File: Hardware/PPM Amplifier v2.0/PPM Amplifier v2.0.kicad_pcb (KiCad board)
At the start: 2 copper layers, 0 parts

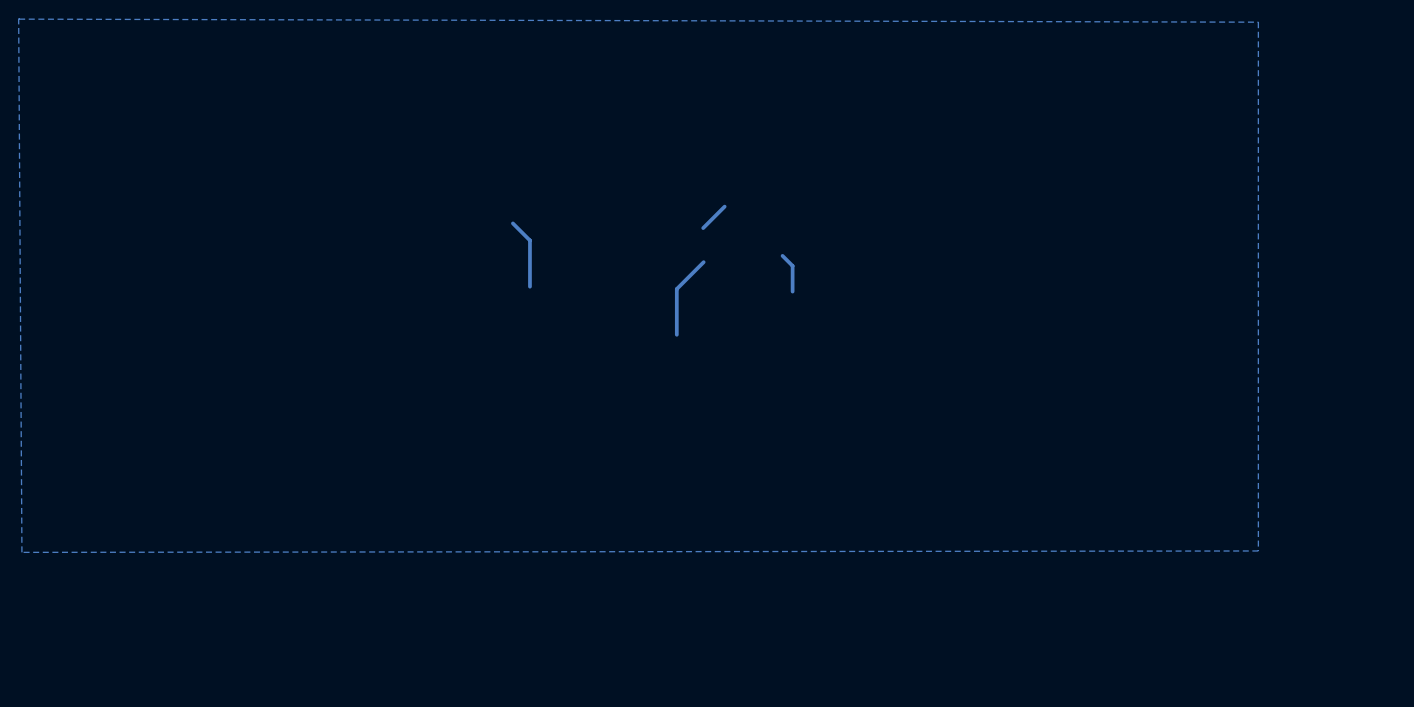
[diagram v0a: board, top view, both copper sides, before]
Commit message: Update PPM Amplifier v2.0 hardware design and add Gerber outputs
Updated KiCad schematic and PCB layout; added fabrication outputs
(Gerber files, drill files, PCBWay BOM/positions/netlist).

Co-Authored-By: Claude Sonnet 4.6 <noreply@anthropic.com>
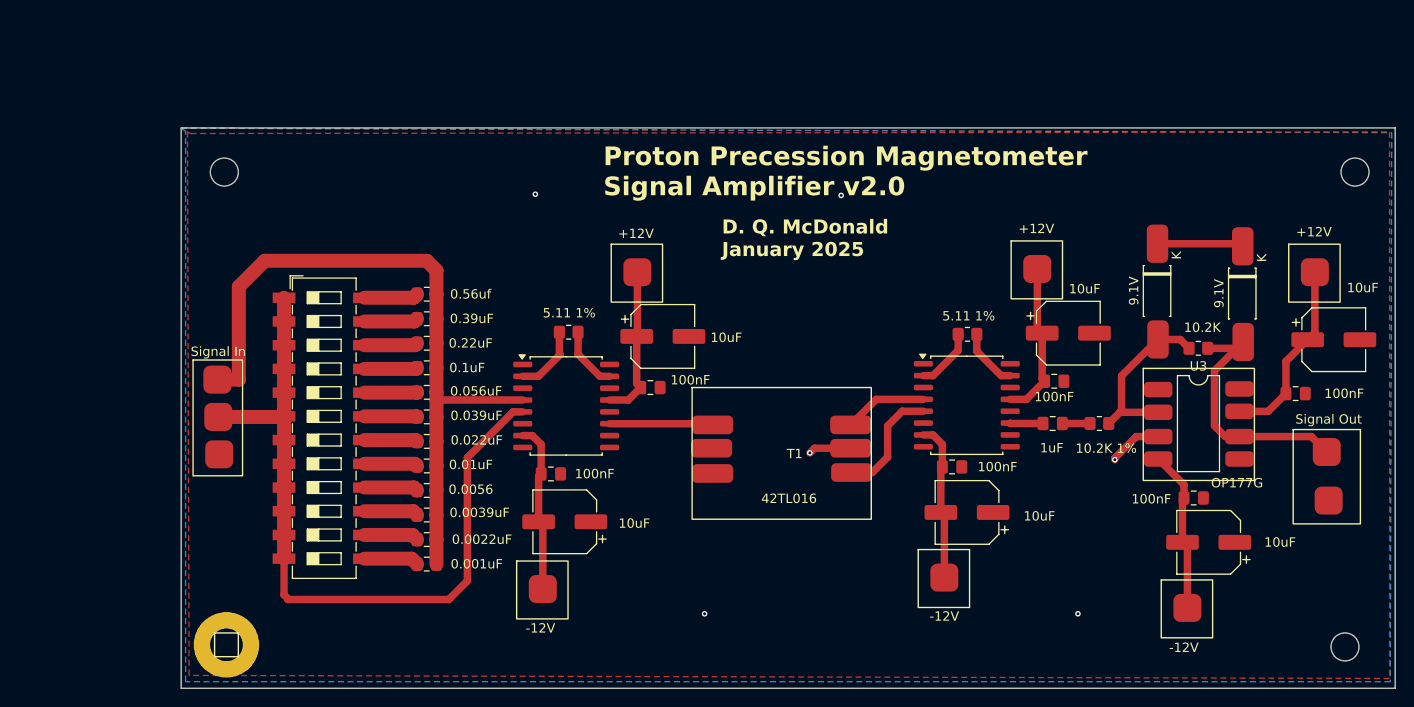
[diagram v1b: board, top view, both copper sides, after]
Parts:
- added C1: 0.56uf, Capacitor_SMD:C_0805_2012Metric_Pad1.18x1.45mm_HandSolder, F.Cu at (70.1, 49.3)
- added C10: 0.0039uF, Capacitor_SMD:C_0805_2012Metric_Pad1.18x1.45mm_HandSolder, F.Cu at (70.1, 72.9)
- added C11: 0.0022uF, Capacitor_SMD:C_0805_2012Metric_Pad1.18x1.45mm_HandSolder, F.Cu at (70.1, 75.5)
- added C12: 0.001uF, Capacitor_SMD:C_0805_2012Metric_Pad1.18x1.45mm_HandSolder, F.Cu at (70.1, 78.2)
- added C13: 10uF, Capacitor_SMD:CP_Elec_6.3x5.2, F.Cu at (95.4, 53.8)
- added C14: 10uF, Capacitor_SMD:CP_Elec_6.3x5.2, F.Cu at (84.9, 73.6)
- added C15: 10uF, Capacitor_SMD:CP_Elec_6.3x5.2, F.Cu at (138.8, 53.4)
- added C16: 10uF, Capacitor_SMD:CP_Elec_6.3x5.2, F.Cu at (167.2, 54.1)
- added C17: 1uF, Capacitor_SMD:C_0805_2012Metric_Pad1.18x1.45mm_HandSolder, F.Cu at (137.1, 63.1)
- added C18: 10uF, Capacitor_SMD:CP_Elec_6.3x5.2, F.Cu at (128.0, 72.6)
- added C19: 10uF, Capacitor_SMD:CP_Elec_6.3x5.2, F.Cu at (153.8, 75.8)
- added C2: 0.39uF, Capacitor_SMD:C_0805_2012Metric_Pad1.18x1.45mm_HandSolder, F.Cu at (70.1, 51.9)
- added C20: 100nF, Capacitor_SMD:C_0805_2012Metric_Pad1.18x1.45mm_HandSolder, F.Cu at (94.0, 59.2)
- added C21: 100nF, Capacitor_SMD:C_0805_2012Metric_Pad1.18x1.45mm_HandSolder, F.Cu at (83.4, 68.5)
- added C22: 100nF, Capacitor_SMD:C_0805_2012Metric_Pad1.18x1.45mm_HandSolder, F.Cu at (152.2, 71.1)
- added C23: 100nF, Capacitor_SMD:C_0805_2012Metric_Pad1.18x1.45mm_HandSolder, F.Cu at (137.3, 58.6)
- added C24: 100nF, Capacitor_SMD:C_0805_2012Metric_Pad1.18x1.45mm_HandSolder, F.Cu at (163.1, 59.9)
- added C25: 100nF, Capacitor_SMD:C_0805_2012Metric_Pad1.18x1.45mm_HandSolder, F.Cu at (126.3, 67.8)
- added C3: 0.22uF, Capacitor_SMD:C_0805_2012Metric_Pad1.18x1.45mm_HandSolder, F.Cu at (70.1, 54.5)
- added C4: 0.1uF, Capacitor_SMD:C_0805_2012Metric_Pad1.18x1.45mm_HandSolder, F.Cu at (70.1, 57.1)
- added C5: 0.056uF, Capacitor_SMD:C_0805_2012Metric_Pad1.18x1.45mm_HandSolder, F.Cu at (70.1, 59.8)
- added C6: 0.039uF, Capacitor_SMD:C_0805_2012Metric_Pad1.18x1.45mm_HandSolder, F.Cu at (70.1, 62.4)
- added C7: 0.022uF, Capacitor_SMD:C_0805_2012Metric_Pad1.18x1.45mm_HandSolder, F.Cu at (70.1, 65.0)
- added C8: 0.01uF, Capacitor_SMD:C_0805_2012Metric_Pad1.18x1.45mm_HandSolder, F.Cu at (70.1, 67.6)
- added C9: 0.0056, Capacitor_SMD:C_0805_2012Metric_Pad1.18x1.45mm_HandSolder, F.Cu at (70.1, 70.3)
- added D1: 9.1V, DQM:D_DO-41_SMD, F.Cu at (148.3, 45.1)
- added D2: 9.1V, DQM:D_DO-41_SMD, F.Cu at (157.4, 45.4)
- added J1: -12V, DQM:Conn1 SMD, F.Cu at (125.4, 79.7)
- added J2: Signal In, DQM:Conn3 SMD, F.Cu at (47.7, 62.3)
- added J3: +12V, DQM:Conn1 SMD, F.Cu at (135.4, 46.6)
- added J4: +12V, DQM:Conn1 SMD, F.Cu at (165.1, 47.0)
- added J5: +12V, DQM:Conn1 SMD, F.Cu at (92.5, 47.0)
- added J6: -12V, DQM:Conn1 SMD, F.Cu at (82.4, 80.9)
- added J7: -12V, DQM:Conn1 SMD, F.Cu at (151.4, 83.0)
- added J8: GND, DQM:3MM Pad, F.Cu at (48.6, 86.8)
- added P2: Signal Out, DQM:Conn2 SMD, F.Cu at (166.6, 66.2)
- added R1: 5.11 1%, Resistor_SMD:R_0805_2012Metric_Pad1.20x1.40mm_HandSolder, F.Cu at (85.3, 53.3)
- added R2: 5.11 1%, Resistor_SMD:R_0805_2012Metric_Pad1.20x1.40mm_HandSolder, F.Cu at (128.0, 53.5)
- added R3: 10.2K 1%, Resistor_SMD:R_0805_2012Metric_Pad1.20x1.40mm_HandSolder, F.Cu at (142.1, 63.1)
- added R4: 10.2K, Resistor_SMD:R_0805_2012Metric_Pad1.20x1.40mm_HandSolder, F.Cu at (152.7, 55.0)
- added REF**: MountingHole_3mm, MountingHole:MountingHole_3mm, F.Cu at (48.4, 36.2)
- added REF**: MountingHole_3mm, MountingHole:MountingHole_3mm, F.Cu at (168.4, 87.0)
- added REF**: MountingHole_3mm, MountingHole:MountingHole_3mm, F.Cu at (169.5, 36.2)
- added SW1: SW_DIP_x12, Button_Switch_SMD:SW_DIP_SPSTx12_Slide_6.7x32.04mm_W8.61mm_P2.54mm_LowProfile, F.Cu at (59.1, 63.6)
- added T1: 42TL016, DQM:Transformer_42TL016_SMD, F.Cu at (109.0, 66.2)
- added U1: ~, Package_SO:SOIC-16W_7.5x10.3mm_P1.27mm, F.Cu at (85.0, 61.2)
- added U2: ~, Package_SO:SOIC-16W_7.5x10.3mm_P1.27mm, F.Cu at (127.9, 61.1)
- added U3: OP177G, DQM:DIP-8_SMD, F.Cu at (148.9, 59.3)
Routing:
- net Net-(J2-Pin_2): track 0.00 -> 80.8 mm
- net Net-(J2-Pin_1): track 0.00 -> 75.7 mm
- net Net-(D2-A): track 0.00 -> 27.5 mm
- net Net-(J4-Pin_1): track 0.00 -> 20.0 mm
- net Net-(D1-A): track 0.00 -> 18.9 mm
- net Net-(J6-Pin_1): track 0.00 -> 18.1 mm
- net Net-(J7-Pin_1): track 0.00 -> 17.4 mm
- net Net-(J1-Pin_1): track 0.00 -> 16.9 mm
- net Net-(J3-Pin_1): track 0.00 -> 16.8 mm
- net Net-(J5-Pin_1): track 0.00 -> 16.5 mm
- net -12V: track 13.2 -> 0.00 mm
- net GND: track 0.00 -> 10.4 mm, vias 0 -> 6
- net Net-(T1-AA): track 0.00 -> 10.3 mm
- net Net-(D1-K): track 0.00 -> 9.24 mm
- net Net-(T1-6): track 3.25 -> 12.4 mm
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- added copper zone on F.Cu, net GND
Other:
- board outline added: 130 x 60 mm
- board text added: "D. Q. McDonald January 2025"
- board text added: "Proton Precession Magnetometer Signal Amplifier v2.0"
